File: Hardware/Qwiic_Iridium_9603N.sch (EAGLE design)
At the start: 61 parts, among them J1 IRIDIUM_9603N, J10 STANDOFFS_M2X0.4_STEEL_6MM, J3 PTH, J6 ISP, J7 U.FL, J9 STANDOFFS_M2X0.4_STEEL_6MM, Q2 5.8A/30V/35mΩ, U1 ATTINY841SOIC, U2 LTC3225EDDB#TRMPBF, U3 ADM4210-1

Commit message: Adding x02 regular and production files.
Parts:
- removed J10, J9: STANDOFFS_M2X0.4_STEEL_6MM, New_Parts:STANDOFFS_M2X0.4_STEEL_6MM
- C5, C6: device New_Parts:1F-2.7V(PTH)CPOL-RADIAL-1H-2.7V -> SparkFun-Capacitors:1F-2.7V(PTH)CPOL-RADIAL-1H-2.7V
- J1: device New_Parts:IRIDIUM_9603N -> Qwiic_Iridium_9603N:IRIDIUM_9603N
- R1, R12: device SparkFun-Resistors:1KOHM-0603-1/10W-1% -> Qwiic_Iridium_9603N:1KOHM-0603-1/10W-1%
- R9: value 0.012R -> 0.012 Ohm; device New_Parts:RESISTOR_0603_12MILLIOHM0603 -> SparkFun-Resistors:RESISTOR0603
- U1: device New_Parts:ATTINY841SOIC -> Qwiic_Iridium_9603N:ATTINY841SOIC
- U2: device New_Parts:LTC3225EDDB-TRMPBFDFN300X200-10L -> Qwiic_Iridium_9603N:LTC3225EDDB-TRMPBFDFN300X200-10L
- U3: device New_Parts:ADM4210-1 -> Qwiic_Iridium_9603N:ADM4210-1
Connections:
- net GND: now also J1.HOLE1, J1.HOLE2; no longer J10.1, J9.1

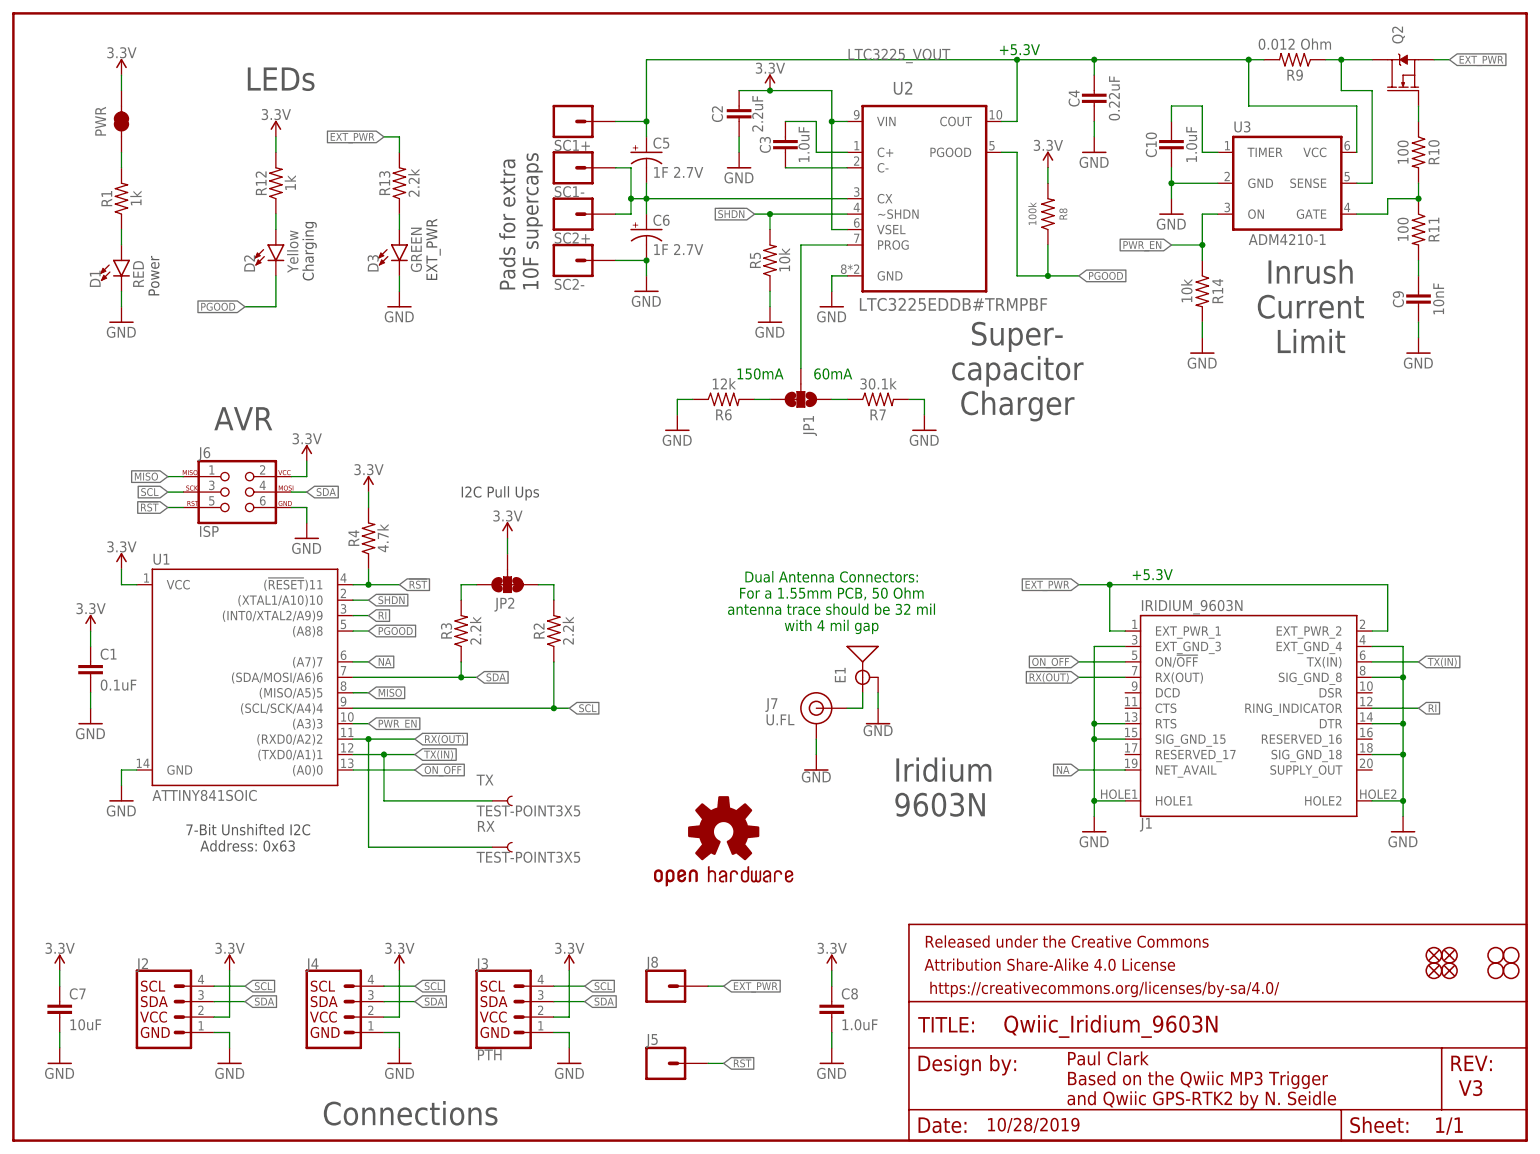
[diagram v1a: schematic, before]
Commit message: X03 Candidate - adds standoffs as separate items for the BOM
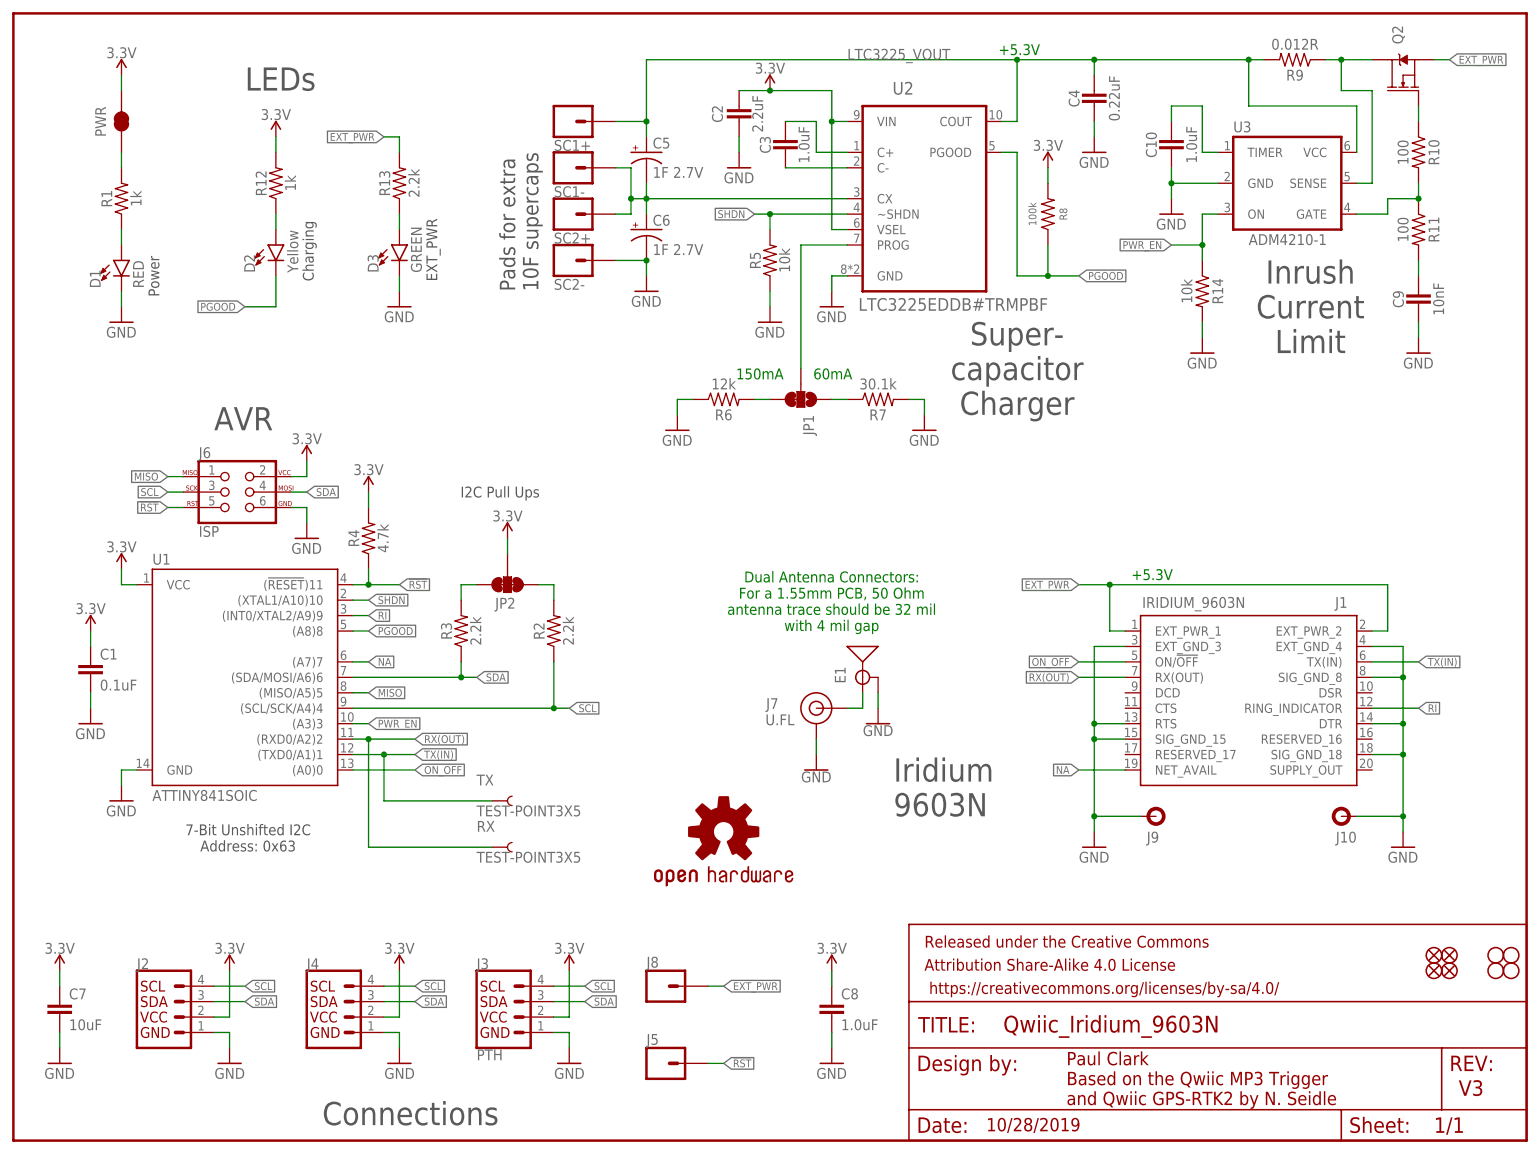
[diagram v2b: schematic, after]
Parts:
- added J10, J9: STANDOFFS_M2X0.4_STEEL_6MM, New_Parts:STANDOFFS_M2X0.4_STEEL_6MM
- C5, C6: device SparkFun-Capacitors:1F-2.7V(PTH)CPOL-RADIAL-1H-2.7V -> New_Parts:1F-2.7V(PTH)CPOL-RADIAL-1H-2.7V
- J1: device Qwiic_Iridium_9603N:IRIDIUM_9603N -> New_Parts:IRIDIUM_9603N
- R1, R12: device Qwiic_Iridium_9603N:1KOHM-0603-1/10W-1% -> SparkFun-Resistors:1KOHM-0603-1/10W-1%
- R9: value 0.012 Ohm -> 0.012R; device SparkFun-Resistors:RESISTOR0603 -> New_Parts:RESISTOR_0603_12MILLIOHM0603
- U1: device Qwiic_Iridium_9603N:ATTINY841SOIC -> New_Parts:ATTINY841SOIC
- U2: device Qwiic_Iridium_9603N:LTC3225EDDB-TRMPBFDFN300X200-10L -> New_Parts:LTC3225EDDB-TRMPBFDFN300X200-10L
- U3: device Qwiic_Iridium_9603N:ADM4210-1 -> New_Parts:ADM4210-1
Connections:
- net GND: now also J10.1, J9.1; no longer J1.HOLE1, J1.HOLE2
